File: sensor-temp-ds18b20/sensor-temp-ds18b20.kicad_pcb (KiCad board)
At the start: 2 copper layers, 29.6 x 27.7 mm, 9 parts, among them J1 PWR & Sensor, J2 ESP-01S, J3 TempSensor, J4 Conn_01x03_Pin, U1 LMZM23601V3SILR

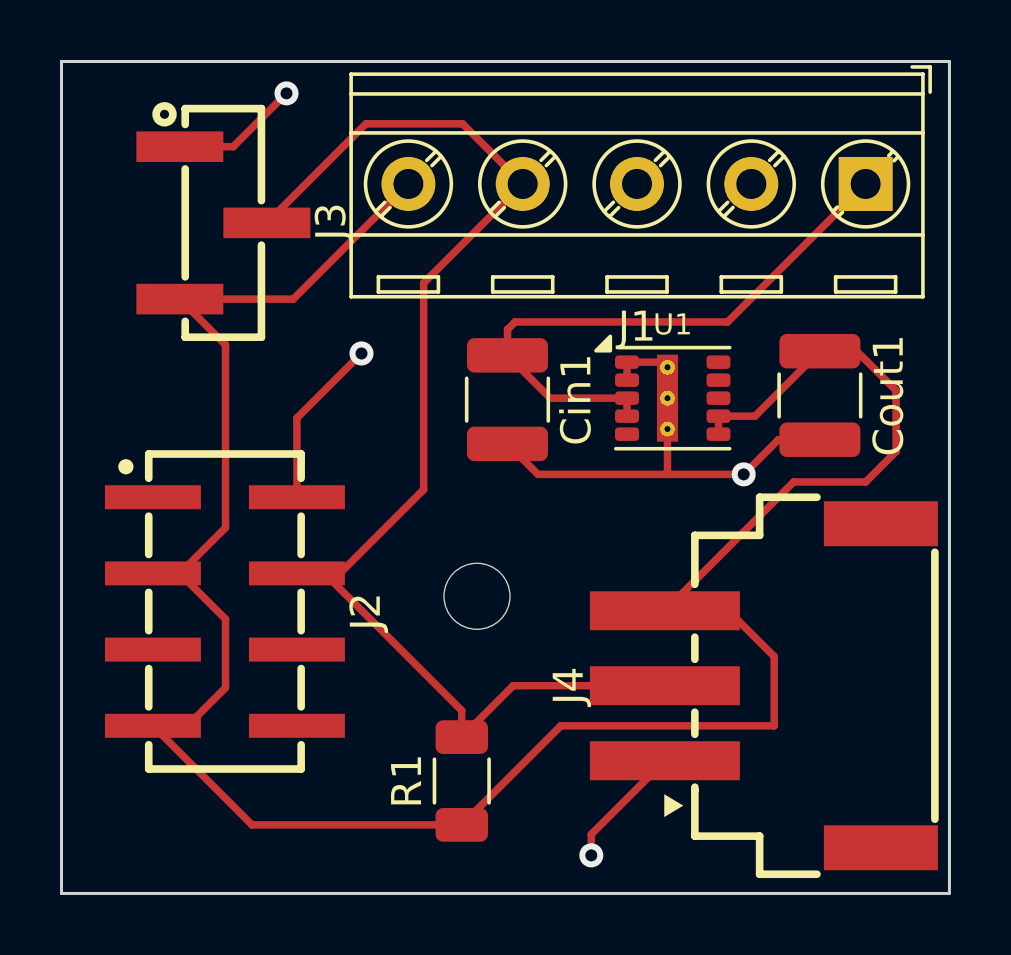
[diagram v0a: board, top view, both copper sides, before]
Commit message: Added reverse polarity protection and fixed the footprint paths
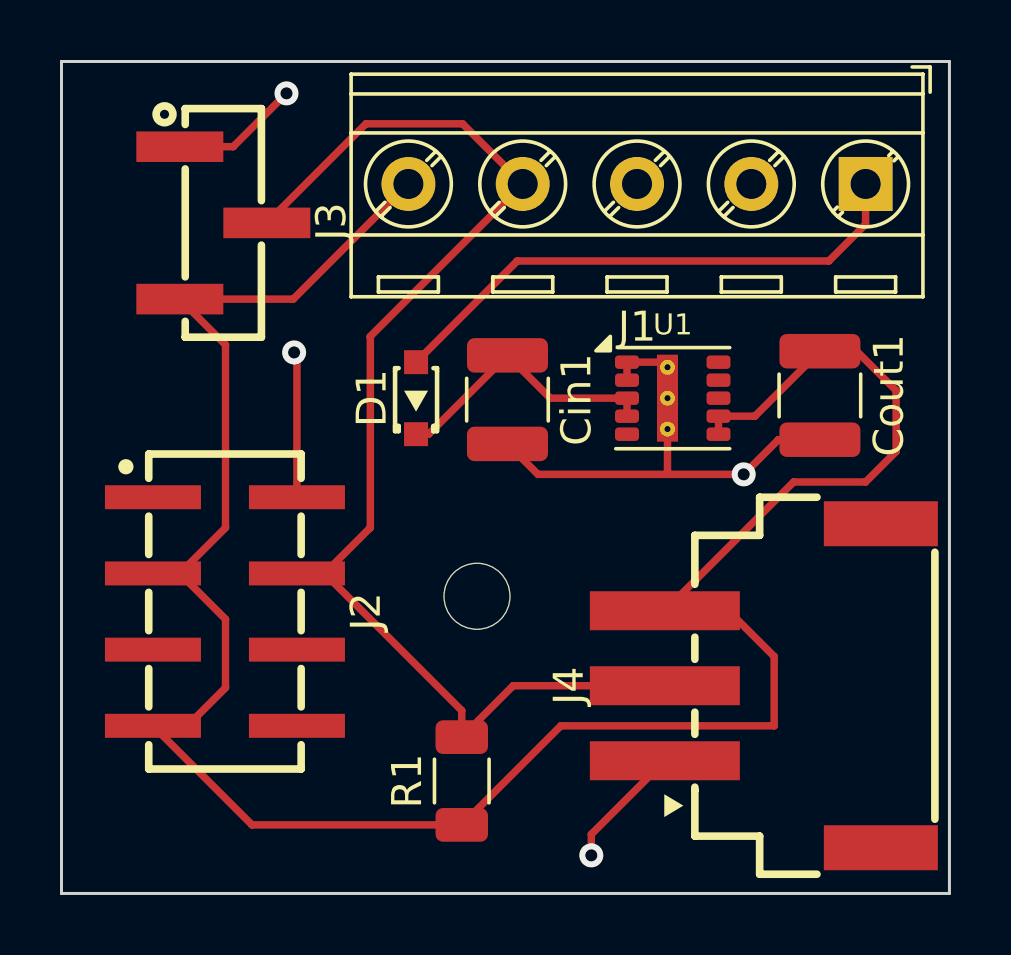
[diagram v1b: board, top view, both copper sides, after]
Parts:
- added D1: D, C5174649:SOD-323_L1.7-W1.3-LS2.5-RD, F.Cu at (123.7, 86.4)
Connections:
- Cin1 pad 1: Net-(J1-Vin) -> Net-(D1-K)
- J1 pad 1: Net-(J1-Vin) -> Net-(D1-A)
- U1 pad 3: Net-(J1-Vin) -> Net-(D1-K)
- U1 pad 4: Net-(J1-Vin) -> Net-(D1-K)
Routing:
- net Net-(J1-Vin): track 20.0 -> 0.00 mm
- net Net-(D1-A): track 0.00 -> 18.2 mm
- net Net-(D1-K): track 0.00 -> 9.31 mm
- net Net-(J1-TempData): track 43.4 -> 42.2 mm
- net Earth: track 30.0 -> 29.2 mm
